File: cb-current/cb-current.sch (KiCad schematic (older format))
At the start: 34 parts, among them P1 CONN_3, P2 CONN_3, P3 CONN_3, P4 CONN_01X09, P5 CONN_01X02, P6 CONN_01X01, P7 CONN_01X01, P8 CONN_01X01, SW1 SW_PUSH_SMALL, U1 MCP1700-3.0

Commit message: Drive current circuits from MCU pins
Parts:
- PS1: symbol PANSTAMP_NRG2 -> PANSTAMP_NRG2-RESCUE-cb-current
- R11, R12: value 470k -> 1M
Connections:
- net D20: now also R1.2
- net D21: now also R3.2
- net D22: now also R7.2
- net VCC: no longer R1.2, R3.2, R7.2
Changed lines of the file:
@@
 EESchema Schematic File Version 2
+LIBS:cb-current-rescue
 LIBS:power
 LIBS:device
@@
 LIBS:memory
 LIBS:xilinx
-LIBS:special
 LIBS:microcontrollers
 LIBS:dsp
@@
 	7150 3000 7500 3000
 $Comp
-L PANSTAMP_NRG2 PS1
+L PANSTAMP_NRG2-RESCUE-cb-current PS1
 U 1 1 552D08E5
 P 2550 2050
@@
 Text Label 3950 1300 2    60   ~ 0
 TOANT
-$Comp
-L VCC #PWR015
-U 1 1 552D08F1
-P 1150 4100
-F 0 "#PWR015" H 1150 4200 30  0001 C CNN
-F 1 "VCC" H 1150 4200 30  0000 C CNN
-F 2 "" H 1150 4100 60  0001 C CNN
-F 3 "" H 1150 4100 60  0001 C CNN
-	1    1150 4100
-	1    0    0    -1
-$EndComp
-$Comp
-L VCC #PWR016
-U 1 1 552D08F2
-P 1150 5750
-F 0 "#PWR016" H 1150 5850 30  0001 C CNN
-F 1 "VCC" H 1150 5850 30  0000 C CNN
-F 2 "" H 1150 5750 60  0001 C CNN
-F 3 "" H 1150 5750 60  0001 C CNN
-	1    1150 5750
-	1    0    0    -1
-$EndComp
-$Comp
-L VCC #PWR017
-U 1 1 552D08F3
-P 3250 4100
-F 0 "#PWR017" H 3250 4200 30  0001 C CNN
-F 1 "VCC" H 3250 4200 30  0000 C CNN
-F 2 "" H 3250 4100 60  0001 C CNN
-F 3 "" H 3250 4100 60  0001 C CNN
-	1    3250 4100
-	1    0    0    -1
-$EndComp
 Text Label 1100 1850 0    60   ~ 0
 A0
@@
 $EndComp
 $Comp
-L GND #PWR018
+L GND #PWR015
 U 1 1 552D0926
 P 4350 6750
-F 0 "#PWR018" H 4350 6750 30  0001 C CNN
+F 0 "#PWR015" H 4350 6750 30  0001 C CNN
 F 1 "GND" H 4350 6680 30  0001 C CNN
 F 2 "" H 4350 6750 60  0001 C CNN
@@
 Connection ~ 4350 6300
 $Comp
-L GND #PWR019
+L GND #PWR016
 U 1 1 552D0928
 P 4900 6750
-F 0 "#PWR019" H 4900 6750 30  0001 C CNN
+F 0 "#PWR016" H 4900 6750 30  0001 C CNN
 F 1 "GND" H 4900 6680 30  0001 C CNN
 F 2 "" H 4900 6750 60  0001 C CNN
@@
 	4900 6750 4900 6600
 $Comp
-L VCC #PWR020
+L VCC #PWR017
 U 1 1 552D0929
 P 6100 6200
-F 0 "#PWR020" H 6100 6300 30  0001 C CNN
+F 0 "#PWR017" H 6100 6300 30  0001 C CNN
 F 1 "VCC" H 6100 6300 30  0000 C CNN
 F 2 "" H 6100 6200 60  0000 C CNN
@@
 	4000 6200 4000 6400
 $Comp
-L GND #PWR021
+L GND #PWR018
 U 1 1 552D2F85
 P 4000 6750
-F 0 "#PWR021" H 4000 6750 30  0001 C CNN
+F 0 "#PWR018" H 4000 6750 30  0001 C CNN
 F 1 "GND" H 4000 6680 30  0001 C CNN
 F 2 "" H 4000 6750 60  0001 C CNN
@@
 Connection ~ 4000 6300
 $Comp
-L GND #PWR022
+L GND #PWR019
 U 1 1 552D3275
 P 5750 6750
-F 0 "#PWR022" H 5750 6750 30  0001 C CNN
+F 0 "#PWR019" H 5750 6750 30  0001 C CNN
 F 1 "GND" H 5750 6680 30  0001 C CNN
 F 2 "" H 5750 6750 60  0001 C CNN
@@
 	5750 6750 5750 6700
 $Comp
-L GND #PWR023
+L GND #PWR020
 U 1 1 552D3282
 P 5400 6750
-F 0 "#PWR023" H 5400 6750 30  0001 C CNN
+F 0 "#PWR020" H 5400 6750 30  0001 C CNN
 F 1 "GND" H 5400 6680 30  0001 C CNN
 F 2 "" H 5400 6750 60  0001 C CNN
@@
 $EndComp
 $Comp
-L GND #PWR024
+L GND #PWR021
 U 1 1 552D341D
 P 6100 6750
-F 0 "#PWR024" H 6100 6750 30  0001 C CNN
+F 0 "#PWR021" H 6100 6750 30  0001 C CNN
 F 1 "GND" H 6100 6680 30  0001 C CNN
 F 2 "" H 6100 6750 60  0001 C CNN
@@
 	5400 6400 5400 6300
 $Comp
-L +BATT #PWR025
+L +BATT #PWR022
 U 1 1 552D3F2F
 P 4000 6200
-F 0 "#PWR025" H 4000 6050 60  0001 C CNN
+F 0 "#PWR022" H 4000 6050 60  0001 C CNN
 F 1 "+BATT" H 4000 6340 60  0000 C CNN
 F 2 "" H 4000 6200 60  0000 C CNN
@@
 $EndComp
 $Comp
-L +BATT #PWR026
+L +BATT #PWR023
 U 1 1 552D4044
 P 3450 6050
-F 0 "#PWR026" H 3450 5900 60  0001 C CNN
+F 0 "#PWR023" H 3450 5900 60  0001 C CNN
 F 1 "+BATT" H 3450 6190 60  0000 C CNN
 F 2 "" H 3450 6050 60  0000 C CNN
@@
 $EndComp
 $Comp
-L +BATT #PWR027
+L +BATT #PWR024
 U 1 1 552D62A1
 P 3100 6050
-F 0 "#PWR027" H 3100 5900 60  0001 C CNN
+F 0 "#PWR024" H 3100 5900 60  0001 C CNN
 F 1 "+BATT" H 3100 6190 60  0000 C CNN
 F 2 "" H 3100 6050 60  0000 C CNN
@@
 	3100 6350 3100 6050
 $Comp
-L GND #PWR028
+L GND #PWR025
 U 1 1 552D6367
 P 3100 6750
-F 0 "#PWR028" H 3100 6750 30  0001 C CNN
+F 0 "#PWR025" H 3100 6750 30  0001 C CNN
 F 1 "GND" H 3100 6680 30  0001 C CNN
 F 2 "" H 3100 6750 60  0000 C CNN
@@
 Connection ~ 9700 4800
 $Comp
-L GND #PWR029
+L GND #PWR026
 U 1 1 55313E3E
 P 9700 5400
-F 0 "#PWR029" H 9700 5400 30  0001 C CNN
+F 0 "#PWR026" H 9700 5400 30  0001 C CNN
 F 1 "GND" H 9700 5330 30  0001 C CNN
 F 2 "" H 9700 5400 60  0001 C CNN
@@
 P 9700 5100
 F 0 "R12" V 9780 5100 50  0000 C CNN
-F 1 "470k" V 9700 5100 50  0000 C CNN
+F 1 "1M" V 9700 5100 50  0000 C CNN
 F 2 "old_mysmd:SM0603S" H 9700 5100 60  0001 C CNN
 F 3 "" H 9700 5100 60  0001 C CNN
@@
 P 9700 4500
 F 0 "R11" V 9780 4500 50  0000 C CNN
-F 1 "470k" V 9700 4500 50  0000 C CNN
+F 1 "1M" V 9700 4500 50  0000 C CNN
 F 2 "old_mysmd:SM0603S" H 9700 4500 60  0001 C CNN
 F 3 "" H 9700 4500 60  0001 C CNN
@@
 	9700 4800 10000 4800
 $Comp
-L +BATT #PWR030
+L +BATT #PWR027
 U 1 1 55314323
 P 9700 4200
-F 0 "#PWR030" H 9700 4050 60  0001 C CNN
+F 0 "#PWR027" H 9700 4050 60  0001 C CNN
 F 1 "+BATT" H 9700 4340 60  0000 C CNN
 F 2 "" H 9700 4200 60  0000 C CNN
@@
 	1    0    0    -1
 $EndComp
+Wire Wire Line
+	3250 4100 3000 4100
+Wire Wire Line
+	1150 4100 900  4100
+Wire Wire Line
+	1150 5750 900  5750
+Text Label 900  4100 0    60   ~ 0
+D20
+Text Label 900  5750 0    60   ~ 0
+D21
+Text Label 3000 4100 0    60   ~ 0
+D22
 $EndSCHEMATC

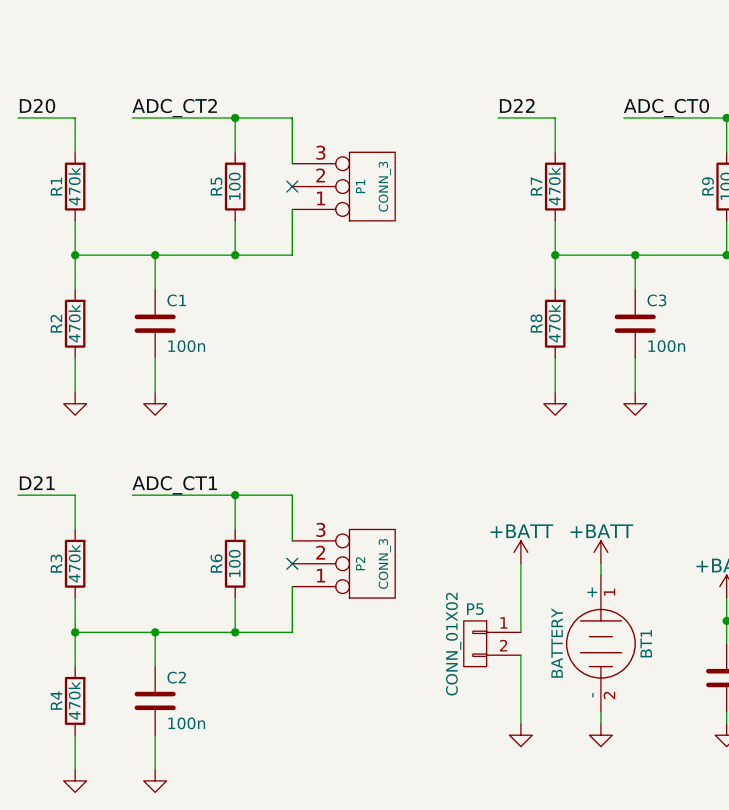
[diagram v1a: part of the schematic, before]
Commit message: voltage divider resistors changed to 10K for current channels
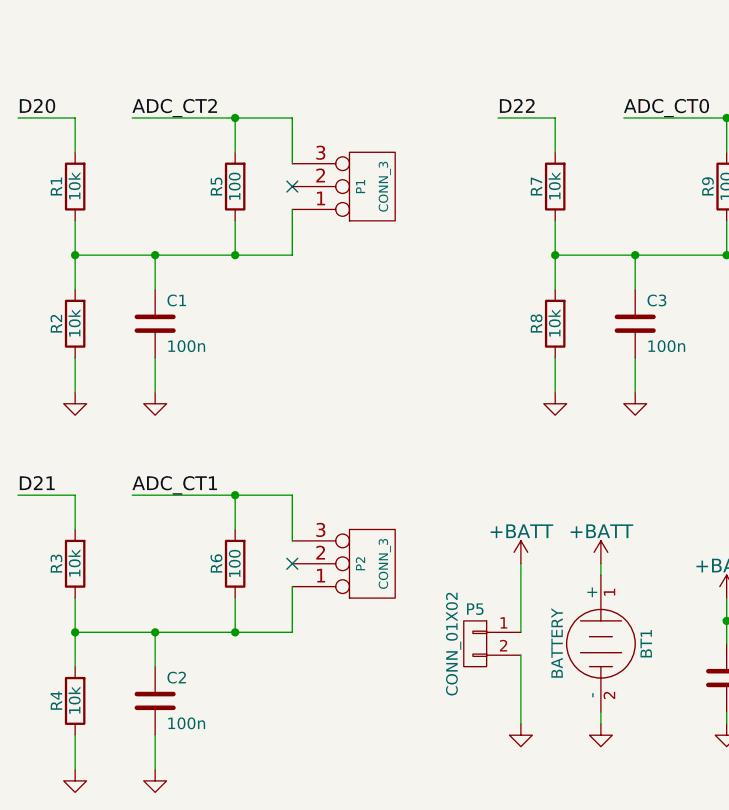
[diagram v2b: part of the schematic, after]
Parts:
- R1, R2, R3, R4, R7, R8: value 470k -> 10k
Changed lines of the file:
@@
 EESchema Schematic File Version 2
-LIBS:cb-current-rescue
 LIBS:power
 LIBS:device
@@
 LIBS:contrib
 LIBS:valves
-LIBS:atmega8
-LIBS:atmel89cxxxx
-LIBS:atmel-1
-LIBS:atmel-2005
-LIBS:avr
-LIBS:avr-1
-LIBS:avr-2
-LIBS:avr-3
-LIBS:avr-4
-LIBS:hopf
-LIBS:rfm-ash
-LIBS:mycomponents
-LIBS:mcp120-130
-LIBS:mcp3304
-LIBS:microchip_mcp2120
-LIBS:microchip-mcp125x-xxx
-LIBS:toshiba
 LIBS:cb-current-cache
 EELAYER 25 0
@@
 Sheet 1 1
 Title "Current meter board for panStamp"
-Date "14 Apr 2015"
-Rev "1.0"
+Date "2017-03-14"
+Rev "1.1"
 Comp "www.panstamp.com"
 Comment1 ""
@@
 P 3250 5000
 F 0 "R8" V 3330 5000 50  0000 C CNN
-F 1 "470k" V 3250 5000 50  0000 C CNN
+F 1 "10k" V 3250 5000 50  0000 C CNN
 F 2 "old_mysmd:SM0603S" H 3250 5000 60  0001 C CNN
 F 3 "" H 3250 5000 60  0001 C CNN
@@
 P 3250 4400
 F 0 "R7" V 3330 4400 50  0000 C CNN
-F 1 "470k" V 3250 4400 50  0000 C CNN
+F 1 "10k" V 3250 4400 50  0000 C CNN
 F 2 "old_mysmd:SM0603S" H 3250 4400 60  0001 C CNN
 F 3 "" H 3250 4400 60  0001 C CNN
@@
 P 1150 6650
 F 0 "R4" V 1230 6650 50  0000 C CNN
-F 1 "470k" V 1150 6650 50  0000 C CNN
+F 1 "10k" V 1150 6650 50  0000 C CNN
 F 2 "old_mysmd:SM0603S" H 1150 6650 60  0001 C CNN
 F 3 "" H 1150 6650 60  0001 C CNN
@@
 P 1150 6050
 F 0 "R3" V 1230 6050 50  0000 C CNN
-F 1 "470k" V 1150 6050 50  0000 C CNN
+F 1 "10k" V 1150 6050 50  0000 C CNN
 F 2 "old_mysmd:SM0603S" H 1150 6050 60  0001 C CNN
 F 3 "" H 1150 6050 60  0001 C CNN
@@
 P 1150 4400
 F 0 "R1" V 1230 4400 50  0000 C CNN
-F 1 "470k" V 1150 4400 50  0000 C CNN
+F 1 "10k" V 1150 4400 50  0000 C CNN
 F 2 "old_mysmd:SM0603S" H 1150 4400 60  0001 C CNN
 F 3 "" H 1150 4400 60  0001 C CNN
@@
 P 1150 5000
 F 0 "R2" V 1230 5000 50  0000 C CNN
-F 1 "470k" V 1150 5000 50  0000 C CNN
+F 1 "10k" V 1150 5000 50  0000 C CNN
 F 2 "old_mysmd:SM0603S" H 1150 5000 60  0001 C CNN
 F 3 "" H 1150 5000 60  0001 C CNN
